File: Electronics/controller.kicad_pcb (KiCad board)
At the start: 2 copper layers, 100 x 100 mm, 129 parts, among them J301 UART, J302 I2C, J501 Switches, J502 Motor Con, J503 Hall Sensor, Q201 IRLZ44N, Q202 IRLIZ44N, Q203 IRLZ44N, Q204 IRLIZ44N, Q205 IRLZ44N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

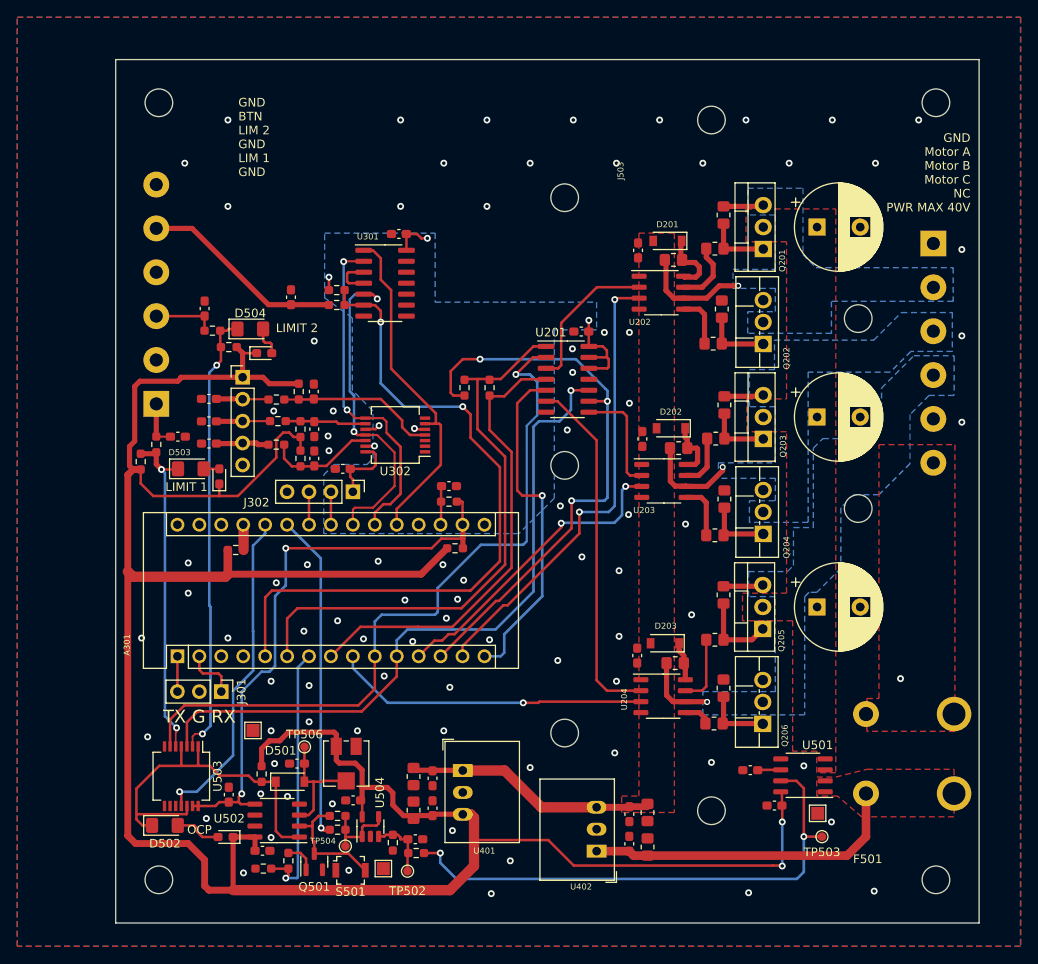
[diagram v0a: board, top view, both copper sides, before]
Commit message: Changed capacitor to multi footprint version. Added parallel diodes to MOSFET gate resistors to improve Turn-OFF time.
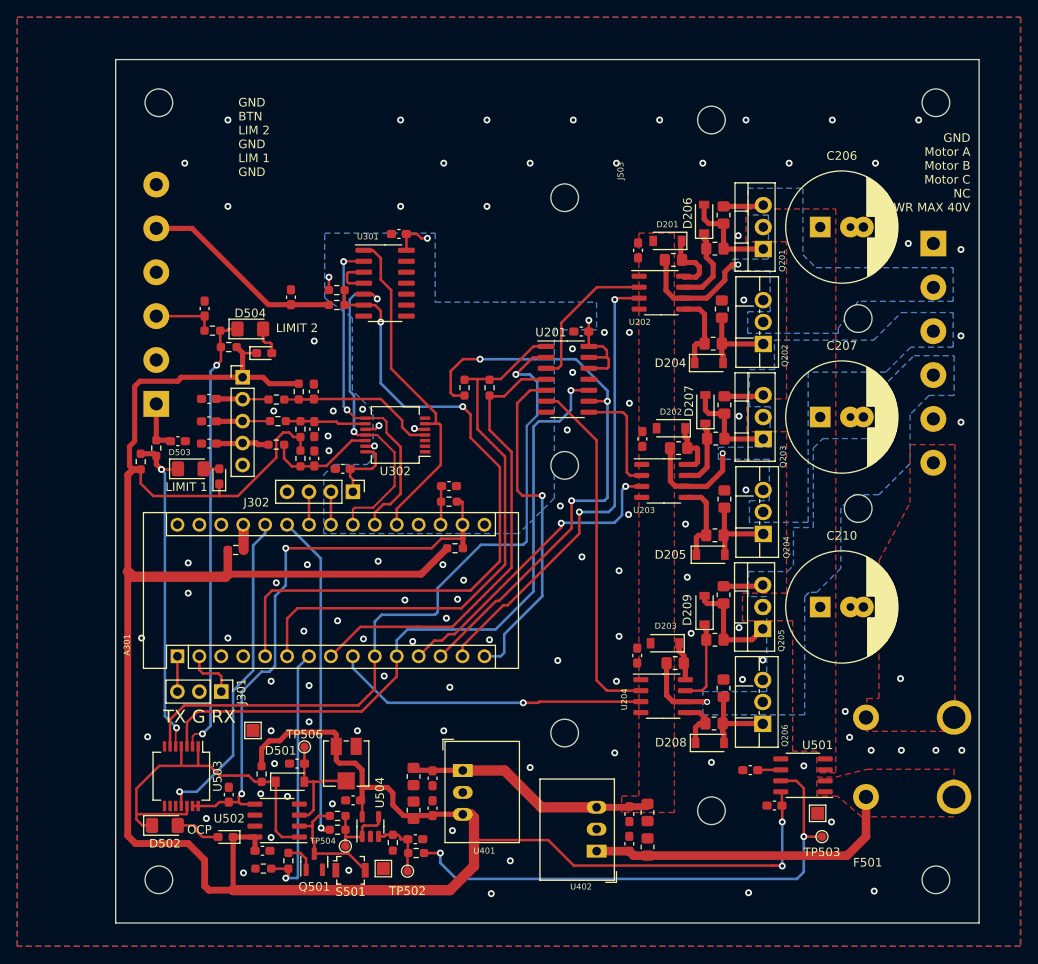
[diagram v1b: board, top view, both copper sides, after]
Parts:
- added D204: 1N5819, Diode_SMD:D_SOD-123, F.Cu at (145.7, 78.2)
- added D205: 1N5819, Diode_SMD:D_SOD-123, F.Cu at (145.9, 100.3)
- added D206: 1N5819, Diode_SMD:D_SOD-123, F.Cu at (145.2, 61.5)
- added D207: 1N5819, Diode_SMD:D_SOD-123, F.Cu at (145.3, 83.5)
- added D208: 1N5819, Diode_SMD:D_SOD-123, F.Cu at (145.8, 122.2)
- added D209: 1N5819, Diode_SMD:D_SOD-123, F.Cu at (145.2, 106.8)
- C206, C207, C210: value C -> 100u; footprint Capacitor_THT:CP_Radial_D10.0mm_P5.00mm -> Findersee_parts:CP_Radial_D12.5mm_P3.5-5.0mm
- moved C501 0.53 mm to (84.2, 87.2)
- moved R501 0.42 mm to (81.7, 88.0)
- moved F501 0.40 mm to (169.0, 123.8)
- moved C206 0.37 mm to (158.6, 62.4)
- moved C207 0.37 mm to (158.6, 84.4)
- moved C210 0.37 mm to (158.6, 106.4)
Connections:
- net /Connectors/LIMIT 1 renamed /Connectors/Limit_1
- net /Connectors/LIMIT 2 renamed /Connectors/Limit_2
- U302 pad 1: unconnected-(U302-Pad1) -> GND
- U302 pad 2: unconnected-(U302-Pad2) -> GND
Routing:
- net Net-(Q201-Pad1): track 7.52 -> 11.6 mm
- net Net-(Q203-Pad1): track 7.42 -> 11.5 mm
- net Net-(R202-Pad2): track 6.37 -> 9.63 mm
- net Net-(R201-Pad2): track 6.07 -> 9.33 mm
- net Net-(R209-Pad2): track 3.20 -> 6.34 mm
- net Net-(Q205-Pad1): track 9.27 -> 12.2 mm
- net Net-(Q204-Pad1): track 7.76 -> 10.1 mm
- net Net-(Q202-Pad1): track 7.81 -> 10.1 mm
- net Net-(Q206-Pad1): track 7.80 -> 10.1 mm
- net Net-(R203-Pad1): track 7.48 -> 9.38 mm
- net Net-(U204-Pad7): track 8.03 -> 9.91 mm
- net Net-(U203-Pad7): track 6.12 -> 7.96 mm
- net /Connectors/MOTOR NEG: track 15.9 -> 17.5 mm
- net /Connectors/MOTOR POS: track 17.2 -> 18.8 mm
- net GND: vias 86 -> 102

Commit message: Manufacturing commit of PCB
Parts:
- added C211: 100n, Capacitor_SMD:C_0603_1608Metric_Pad1.08x0.95mm_HandSolder, F.Cu at (133.2, 105.2)
- added C409: 4u7, Resistor_SMD:R_0805_2012Metric_Pad1.20x1.40mm_HandSolder, F.Cu at (120.8, 57.5)
- added C410: 100n, Capacitor_SMD:C_0603_1608Metric_Pad1.08x0.95mm_HandSolder, F.Cu at (120.5, 59.5)
- added C411: 100n, Capacitor_SMD:C_0603_1608Metric_Pad1.08x0.95mm_HandSolder, F.Cu at (116.9, 59.5)
- added C412: 10u, Resistor_SMD:R_0805_2012Metric_Pad1.20x1.40mm_HandSolder, F.Cu at (117.0, 57.5)
- added R215: 0, Resistor_SMD:R_0603_1608Metric_Pad0.98x0.95mm_HandSolder, F.Cu at (124.6, 114.5)
- added R216: 0, Resistor_SMD:R_0603_1608Metric_Pad0.98x0.95mm_HandSolder, F.Cu at (135.3, 118.2)
- added R217: 0, Resistor_SMD:R_0603_1608Metric_Pad0.98x0.95mm_HandSolder, F.Cu at (129.0, 106.2)
- added R218: 0, Resistor_SMD:R_0603_1608Metric_Pad0.98x0.95mm_HandSolder, F.Cu at (113.7, 114.9)
- added U205: 74LS08, Package_SO:SO-14_3.9x8.65mm_P1.27mm, F.Cu at (130.7, 111.6)
- added U400: R-78C3.3-1.0, Converter_DCDC:Converter_DCDC_RECOM_R-78E-0.5_THT, F.Cu at (120.8, 63.0)
- C201: value C -> 100n
- moved R505 41.5 mm to (80.6, 116.7), turned to 0 degrees
- moved R504 25.5 mm to (80.6, 115.1), turned to 0 degrees
- moved R213 11.0 mm to (121.7, 70.9), turned to 0 degrees
- moved R214 7.05 mm to (123.4, 74.7), turned to 180 degrees
- moved C201 5.33 mm to (130.9, 69.2)
- moved U201 5.33 mm to (129.3, 74.7)
- moved R501 0.70 mm to (81.7, 88.7)
- moved R502 0.10 mm to (88.2, 74.5)
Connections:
- A301 pad 12: /Hbridge/LIN B -> /Hbridge/HIN A
- A301 pad 13: /Hbridge/HIN B -> /Hbridge/LIN A
- A301 pad 14: /Hbridge/LIN A -> /Hbridge/HIN B
- A301 pad 15: /Hbridge/C LIMIT -> /Hbridge/A CTRL
- A301 pad 16: unconnected-(A301-Pad16) -> /Hbridge/C CTRL
- A301 pad 6: /Hbridge/HIN A -> /Hbridge/LIN B
- D503 pad 1: /Connectors/Limit_1 -> Net-(C501-Pad1)
- D504 pad 1: /Connectors/Limit_2 -> Net-(C502-Pad1)
- U201 pad 12: +3V3 -> GND
- U201 pad 13: +3V3 -> GND
- U201 pad 5: /Hbridge/C LIMIT -> /Hbridge/C CTRL
- U202 pad 3: /Hbridge/LIN A -> Net-(U205-Pad3)
- U203 pad 3: /Hbridge/LIN B -> Net-(U203-Pad3)
- U204 pad 3: /Hbridge/LIN C -> Net-(U204-Pad3)
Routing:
- net Net-(U205-Pad3): track 0.00 -> 54.2 mm
- net VDD: track 294.3 -> 348.1 mm
- net /Hbridge/C LIMIT: track 39.7 -> 0.00 mm, vias 1 -> 0
- net Net-(U203-Pad3): track 0.00 -> 32.6 mm, vias 0 -> 2
- net VCC: track 28.8 -> 61.2 mm
- net /Hbridge/C CTRL: track 0.00 -> 27.8 mm, vias 0 -> 1
- net +3V3: track 97.0 -> 120.5 mm, vias 8 -> 10
- net /Hbridge/LIN A: track 53.8 -> 31.6 mm, vias 2 -> 0
- net /Hbridge/HIN A: track 66.1 -> 52.9 mm
- net /Hbridge/A CTRL: track 0.00 -> 12.7 mm, vias 0 -> 1
- net Net-(U204-Pad3): track 0.00 -> 10.1 mm
- net /Hbridge/HIN B: track 67.8 -> 59.0 mm, vias 3 -> 2
- net Net-(D501-Pad1): track 43.6 -> 35.4 mm
- net /Connectors/Limit_2: track 51.8 -> 59.6 mm, vias 2 -> 3
- net /Hbridge/LIN C: track 36.4 -> 43.1 mm
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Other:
- board text added: "+5V A B C GND"
- board text added: "3V SCL SDA G"
- board text added: "G SDA SCL 3V"
- board text added: "GND Motor A Motor B Motor C NC VIN"
- board text added: "RX G TX"
- board text added: "VIN MAX 40V"
- board text removed: "GND Motor A Motor B Motor C NC PWR MAX 40V"

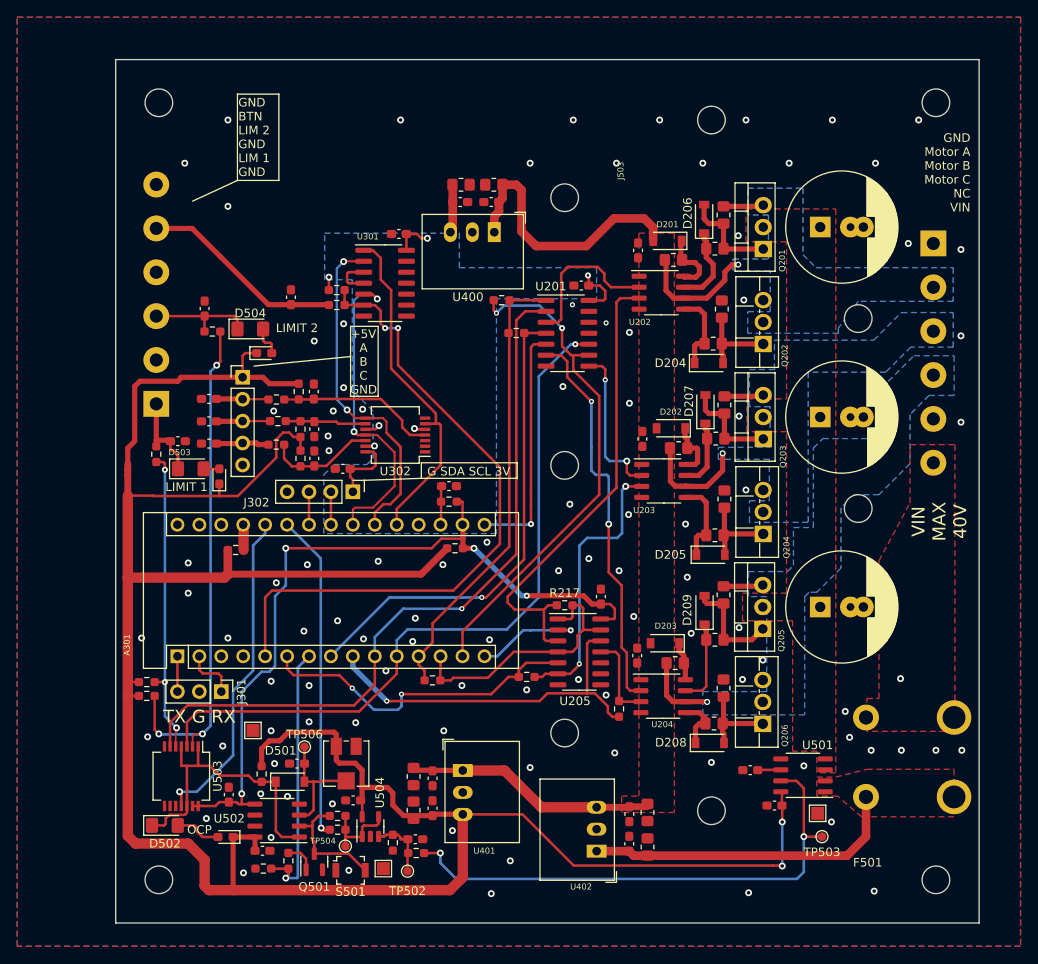
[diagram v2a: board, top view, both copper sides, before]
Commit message: Added STM32 Code for BLDC controller
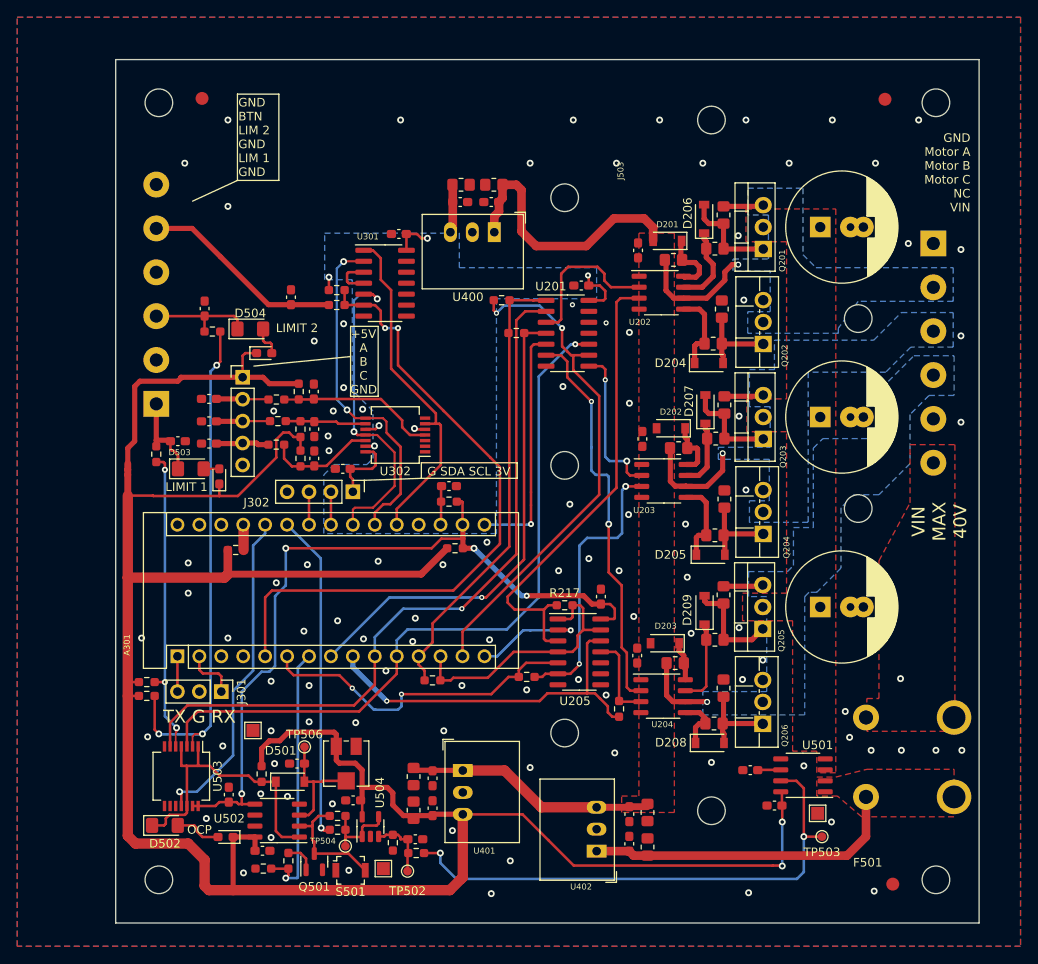
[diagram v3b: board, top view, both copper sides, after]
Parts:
- added FID401: Fiducial, Fiducial:Fiducial_1.5mm_Mask3mm, F.Cu at (166.1, 47.6)
- added FID402: Fiducial, Fiducial:Fiducial_1.5mm_Mask3mm, F.Cu at (167.0, 138.5)
- added FID403: Fiducial, Fiducial:Fiducial_1.5mm_Mask3mm, F.Cu at (87.0, 47.5)
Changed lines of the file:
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@@
   (net 79 "Net-(Q501-Pad3)")
   (net 80 "Net-(R513-Pad1)")
-  (net 81 "Net-(U203-Pad3)")
-  (net 82 "Net-(U204-Pad3)")
+  (net 81 "Net-(R215-Pad1)")
+  (net 82 "Net-(R216-Pad1)")
   (net 83 "unconnected-(U205-Pad8)")
-  (net 84 "Net-(U205-Pad3)")
+  (net 84 "Net-(R217-Pad1)")
   (net 85 "/Hbridge/A CTRL")
   (net 86 "/Hbridge/C CTRL")
@@
       (net 42 "Net-(U201-Pad8)") (pinfunction "HIN") (pintype "input"))
     (pad "3" smd roundrect locked (at -2.575 0.635) (size 1.75 0.6) (layers "F.Cu" "F.Paste" "F.Mask") (roundrect_rratio 0.25)
-      (net 81 "Net-(U203-Pad3)") (pinfunction "LIN") (pintype "input"))
+      (net 81 "Net-(R215-Pad1)") (pinfunction "LIN") (pintype "input"))
     (pad "4" smd roundrect locked (at -2.575 1.905) (size 1.75 0.6) (layers "F.Cu" "F.Paste" "F.Mask") (roundrect_rratio 0.25)
       (net 3 "GND") (pinfunction "COM") (pintype "power_in"))
@@
       (net 41 "Net-(U201-Pad6)") (pinfunction "HIN") (pintype "input"))
     (pad "3" smd roundrect locked (at -2.575 0.635) (size 1.75 0.6) (layers "F.Cu" "F.Paste" "F.Mask") (roundrect_rratio 0.25)
-      (net 82 "Net-(U204-Pad3)") (pinfunction "LIN") (pintype "input"))
+      (net 82 "Net-(R216-Pad1)") (pinfunction "LIN") (pintype "input"))
     (pad "4" smd roundrect locked (at -2.575 1.905) (size 1.75 0.6) (layers "F.Cu" "F.Paste" "F.Mask") (roundrect_rratio 0.25)
       (net 3 "GND") (pinfunction "COM") (pintype "power_in"))
@@
     (fp_line (start 0.8 -0.4125) (end 0.8 0.4125) (layer "F.Fab") (width 0.1))
     (pad "1" smd roundrect locked (at -0.9125 0 180) (size 0.975 0.95) (layers "F.Cu" "F.Paste" "F.Mask") (roundrect_rratio 0.25)
-      (net 81 "Net-(U203-Pad3)") (pintype "passive"))
+      (net 81 "Net-(R215-Pad1)") (pintype "passive"))
     (pad "2" smd roundrect locked (at 0.9125 0 180) (size 0.975 0.95) (layers "F.Cu" "F.Paste" "F.Mask") (roundrect_rratio 0.25)
       (net 15 "/Hbridge/LIN B") (pintype "passive"))
@@
     (pad "" np_thru_hole circle locked (at 0 0) (size 3.2 3.2) (drill 3.2) (layers *.Cu *.Mask))
   )
+  (footprint "Fiducial:Fiducial_1.5mm_Mask3mm" (layer "F.Cu")
+    (at 166.1 47.6)
+    (descr "Circular Fiducial, 1.5mm bare copper, 3mm soldermask opening")
+    (tags "fiducial")
+    (property "Sheetfile" "Power.kicad_sch")
+    (property "Sheetname" "Power")
+    (attr smd)
+    (fp_text reference "FID401" (at 0 -2.4765) (layer "F.SilkS") hide
+      (effects (font (size 1 1) (thickness 0.15)))
+    )
+    (fp_text value "Fiducial" (at 0 2.6035) (layer "F.Fab")
+      (effects (font (size 1 1) (thickness 0.15)))
+    )
+    (fp_text user "${REFERENCE}" (at 0 0) (layer "F.Fab")
+      (effects (font (size 0.4 0.4) (thickness 0.06)))
+    )
+    (fp_circle (center 0 0) (end 1.75 0) (layer "F.CrtYd") (width 0.05) (fill none))
+    (fp_circle (center 0 0) (end 1.5 0) (layer "F.Fab") (width 0.1) (fill none))
+    (pad "" smd circle locked (at 0 0) (size 1.5 1.5) (layers "F.Cu" "F.Mask")
+      (solder_mask_margin 0.75) (clearance 0.75))
+  )
   (footprint "MountingHole:MountingHole_3.2mm_M3_DIN965" (layer "F.Cu")
     (at 146 130)
@@
     (fp_line (start 0.8 -0.4125) (end 0.8 0.4125) (layer "F.Fab") (width 0.1))
     (pad "1" smd roundrect locked (at -0.9125 0 270) (size 0.975 0.95) (layers "F.Cu" "F.Paste" "F.Mask") (roundrect_rratio 0.25)
-      (net 82 "Net-(U204-Pad3)") (pintype "passive"))
+      (net 82 "Net-(R216-Pad1)") (pintype "passive"))
     (pad "2" smd roundrect locked (at 0.9125 0 270) (size 0.975 0.95) (layers "F.Cu" "F.Paste" "F.Mask") (roundrect_rratio 0.25)
       (net 4 "/Hbridge/LIN C") (pintype "passive"))
@@
       (net 85 "/Hbridge/A CTRL") (pintype "input"))
     (pad "3" smd roundrect locked (at -2.475 -1.27) (size 1.95 0.6) (layers "F.Cu" "F.Paste" "F.Mask") (roundrect_rratio 0.25)
-      (net 84 "Net-(U205-Pad3)") (pintype "output"))
+      (net 84 "Net-(R217-Pad1)") (pintype "output"))
     (pad "4" smd roundrect locked (at -2.475 0) (size 1.95 0.6) (layers "F.Cu" "F.Paste" "F.Mask") (roundrect_rratio 0.25)
       (net 18 "/Hbridge/LIN A") (pintype "input"))
@@
       (net 15 "/Hbridge/LIN B") (pintype "input"))
     (pad "6" smd roundrect locked (at -2.475 2.54) (size 1.95 0.6) (layers "F.Cu" "F.Paste" "F.Mask") (roundrect_rratio 0.25)
-      (net 81 "Net-(U203-Pad3)") (pintype "output"))
+      (net 81 "Net-(R215-Pad1)") (pintype "output"))
     (pad "7" smd roundrect locked (at -2.475 3.81) (size 1.95 0.6) (layers "F.Cu" "F.Paste" "F.Mask") (roundrect_rratio 0.25)
       (net 3 "GND") (pinfunction "GND") (pintype "power_in"))
@@
       (net 3 "GND") (pintype "input"))
     (pad "11" smd roundrect locked (at 2.475 0) (size 1.95 0.6) (layers "F.Cu" "F.Paste" "F.Mask") (roundrect_rratio 0.25)
-      (net 82 "Net-(U204-Pad3)") (pintype "output"))
+      (net 82 "Net-(R216-Pad1)") (pintype "output"))
     (pad "12" smd roundrect locked (at 2.475 -1.27) (size 1.95 0.6) (layers "F.Cu" "F.Paste" "F.Mask") (roundrect_rratio 0.25)
       (net 4 "/Hbridge/LIN C") (pintype "input"))
@@
     (fp_line (start 0.8 0.4125) (end -0.8 0.4125) (layer "F.Fab") (width 0.1))
     (pad "1" smd roundrect locked (at -0.9125 0) (size 0.975 0.95) (layers "F.Cu" "F.Paste" "F.Mask") (roundrect_rratio 0.25)
-      (net 84 "Net-(U205-Pad3)") (pintype "passive"))
+      (net 84 "Net-(R217-Pad1)") (pintype "passive"))
     (pad "2" smd roundrect locked (at 0.9125 0) (size 0.975 0.95) (layers "F.Cu" "F.Paste" "F.Mask") (roundrect_rratio 0.25)
       (net 18 "/Hbridge/LIN A") (pintype "passive"))
@@
     )
   )
+  (footprint "Fiducial:Fiducial_1.5mm_Mask3mm" (layer "F.Cu")
+    (at 167 138.5)
+    (descr "Circular Fiducial, 1.5mm bare copper, 3mm soldermask opening")
+    (tags "fiducial")
+    (property "Sheetfile" "Power.kicad_sch")
+    (property "Sheetname" "Power")
+    (attr smd)
+    (fp_text reference "FID402" (at 0 -2.4765) (layer "F.SilkS") hide
+      (effects (font (size 1 1) (thickness 0.15)))
+    )
+    (fp_text value "Fiducial" (at 0 2.6035) (layer "F.Fab")
+      (effects (font (size 1 1) (thickness 0.15)))
+    )
+    (fp_text user "${REFERENCE}" (at 0 0) (layer "F.Fab")
+      (effects (font (size 0.4 0.4) (thickness 0.06)))
+    )
+    (fp_circle (center 0 0) (end 1.75 0) (layer "F.CrtYd") (width 0.05) (fill none))
+    (fp_circle (center 0 0) (end 1.5 0) (layer "F.Fab") (width 0.1) (fill none))
+    (pad "" smd circle locked (at 0 0) (size 1.5 1.5) (layers "F.Cu" "F.Mask")
+      (solder_mask_margin 0.75) (clearance 0.75))
+  )
   (footprint "Package_SO:SO-8_3.9x4.9mm_P1.27mm" (layer "F.Cu")
     (at 140.2 70)
@@
       (net 33 "Net-(U201-Pad3)") (pinfunction "HIN") (pintype "input"))
     (pad "3" smd roundrect locked (at -2.575 0.635) (size 1.75 0.6) (layers "F.Cu" "F.Paste" "F.Mask") (roundrect_rratio 0.25)
-      (net 84 "Net-(U205-Pad3)") (pinfunction "LIN") (pintype "input"))
+      (net 84 "Net-(R217-Pad1)") (pinfunction "LIN") (pintype "input"))
     (pad "4" smd roundrect locked (at -2.575 1.905) (size 1.75 0.6) (layers "F.Cu" "F.Paste" "F.Mask") (roundrect_rratio 0.25)
       (net 3 "GND") (pinfunction "COM") (pintype "power_in"))
@@
     )
   )
+  (footprint "Fiducial:Fiducial_1.5mm_Mask3mm" (layer "F.Cu")
+    (at 87 47.5)
+    (descr "Circular Fiducial, 1.5mm bare copper, 3mm soldermask opening")
+    (tags "fiducial")
+    (property "Sheetfile" "Power.kicad_sch")
+    (property "Sheetname" "Power")
+    (attr smd)
+    (fp_text reference "FID403" (at 0 -2.4765) (layer "F.SilkS") hide
+      (effects (font (size 1 1) (thickness 0.15)))
+    )
+    (fp_text value "Fiducial" (at 0 2.6035) (layer "F.Fab")
+      (effects (font (size 1 1) (thickness 0.15)))
+    )
+    (fp_text user "${REFERENCE}" (at 0 0) (layer "F.Fab")
+      (effects (font (size 0.4 0.4) (thickness 0.06)))
+    )
+    (fp_circle (center 0 0) (end 1.75 0) (layer "F.CrtYd") (width 0.05) (fill none))
+    (fp_circle (center 0 0) (end 1.5 0) (layer "F.Fab") (width 0.1) (fill none))
+    (pad "" smd circle locked (at 0 0) (size 1.5 1.5) (layers "F.Cu" "F.Mask")
+      (solder_mask_margin 0.75) (clearance 0.75))
+  )
   (footprint "Capacitor_SMD:C_0603_1608Metric_Pad1.08x0.95mm_HandSolder" (layer "F.Cu")
